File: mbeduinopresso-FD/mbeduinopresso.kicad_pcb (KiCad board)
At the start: 2 copper layers, 101.6 x 86.4 mm, 37 parts, among them J101 LPCXPRESSO_1769_HEADER, J201 PULSE_J0011_PHY_SIDE, J203 Enet, M201 LOGO_OSHW, P201 SERIAL, P301 12V, SW202 Bootloader, SW203 Reset, U201 USBCONN, U202 CONN_MICROSD, U301 LM7805, U302 1117

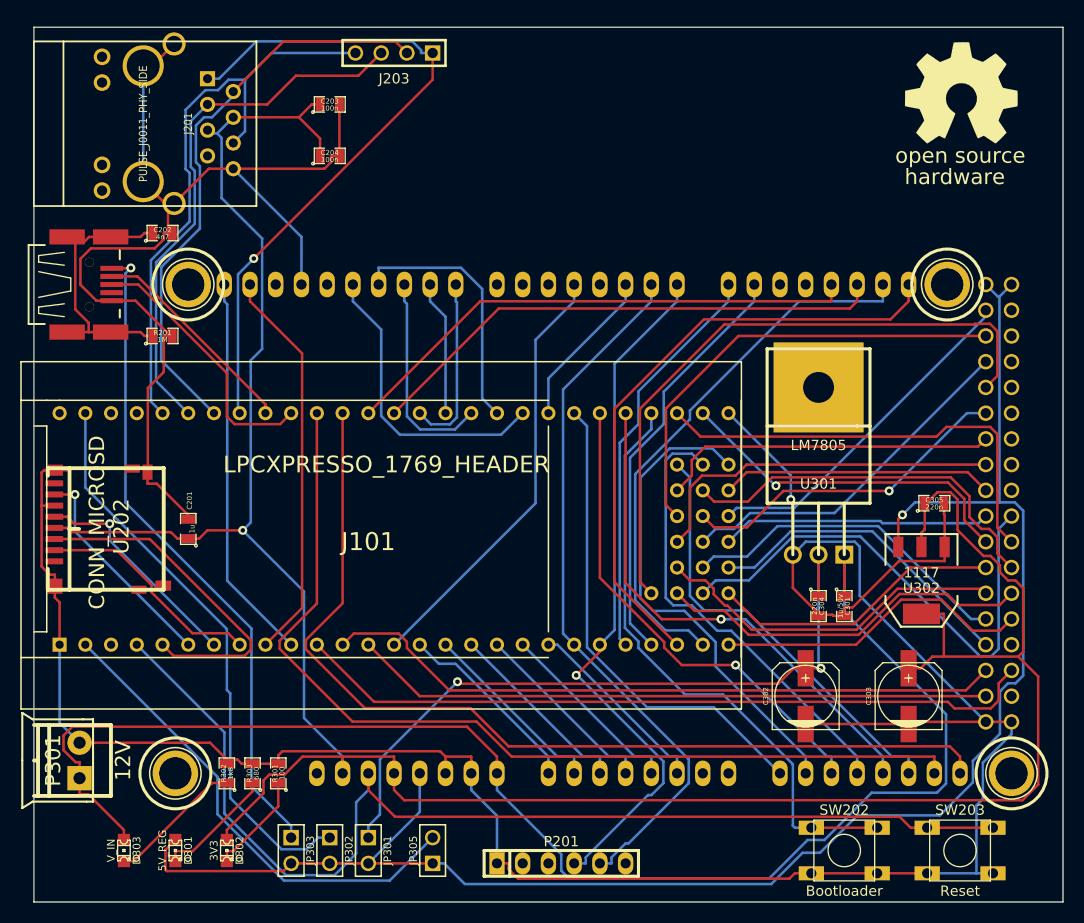
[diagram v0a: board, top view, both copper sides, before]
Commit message: Board size limit 100mm
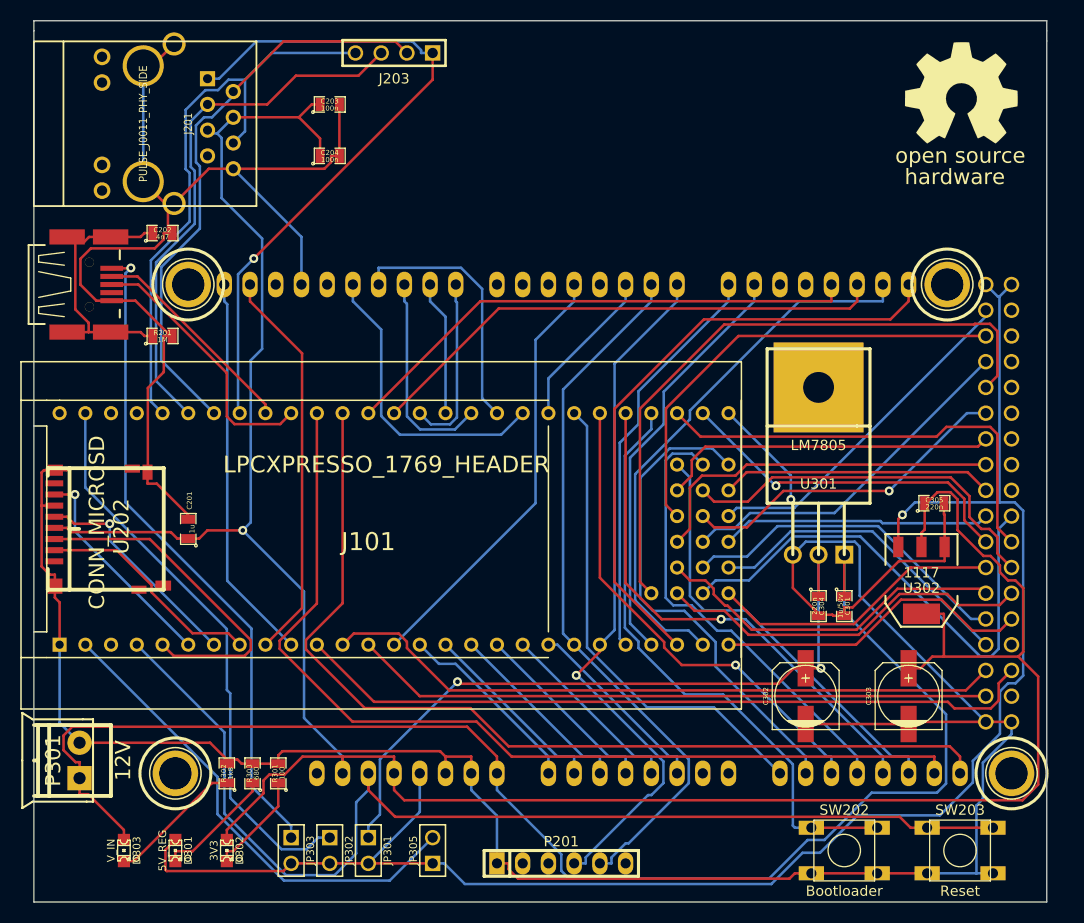
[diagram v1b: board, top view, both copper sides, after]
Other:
- board size 101.6 x 86.4 mm -> 100 x 87 mm
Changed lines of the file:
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@@
     (area 49.149 65.2018 152.819101 152.450001)
     (thickness 1.6)
-    (drawings 4)
+    (drawings 7)
     (tracks 802)
     (zones 0)
@@
     )
   )
-  (gr_line (start 152.4 152.4) (end 50.8 152.4) (angle 90) (layer Edge.Cuts) (width 0.1))
-  (gr_line (start 152.4 66.04) (end 152.4 152.4) (angle 90) (layer Edge.Cuts) (width 0.1))
-  (gr_line (start 50.8 66.04) (end 152.4 66.04) (angle 90) (layer Edge.Cuts) (width 0.1))
-  (gr_line (start 50.8 152.4) (end 50.8 66.04) (angle 90) (layer Edge.Cuts) (width 0.1))
+  (gr_line (start 50.8 65.4) (end 50.8 66.4) (angle 90) (layer Edge.Cuts) (width 0.1))
+  (gr_line (start 150.8 65.4) (end 50.8 65.4) (angle 90) (layer Edge.Cuts) (width 0.1))
+  (gr_line (start 150.8 66.4) (end 150.8 65.4) (angle 90) (layer Edge.Cuts) (width 0.1))
+  (gr_line (start 50.8 66.4) (end 50.8 152.4) (angle 90) (layer Edge.Cuts) (width 0.1))
+  (gr_line (start 150.8 67.4) (end 150.8 66.4) (angle 90) (layer Edge.Cuts) (width 0.1))
+  (gr_line (start 150.8 152.4) (end 150.8 67.4) (angle 90) (layer Edge.Cuts) (width 0.1))
+  (gr_line (start 50.8 152.4) (end 150.8 152.4) (angle 90) (layer Edge.Cuts) (width 0.1))
   (segment (start 127.559 145.07) (end 134.0583 145.07) (width 0.254) (layer F.Cu) (net 1))
   (segment (start 134.0583 145.07) (end 134.059 145.07) (width 0.254) (layer F.Cu) (net 1))
